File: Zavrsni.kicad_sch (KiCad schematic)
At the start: 37 parts, among them K1 JST-2pin-SMD, SW1 SW_Push, SW2 SW_Push

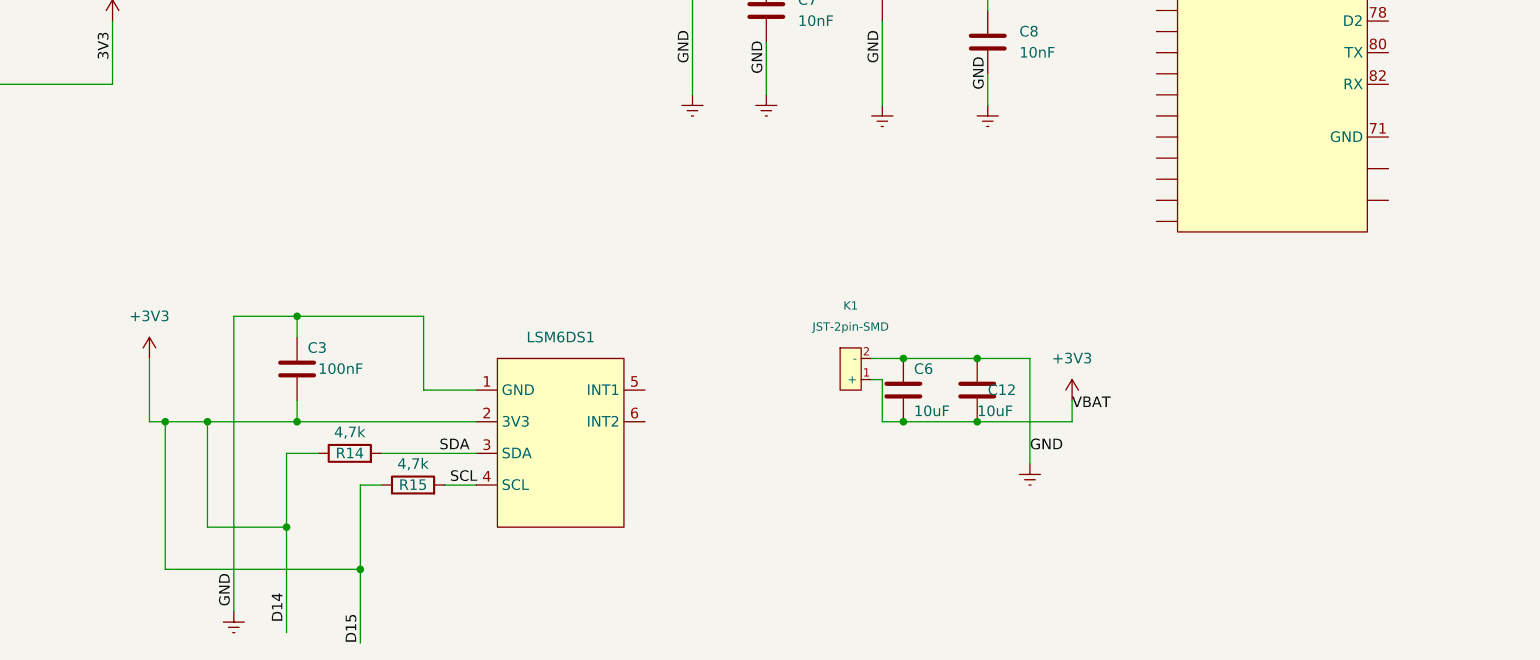
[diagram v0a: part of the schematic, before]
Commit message: All components on the PCB are connected
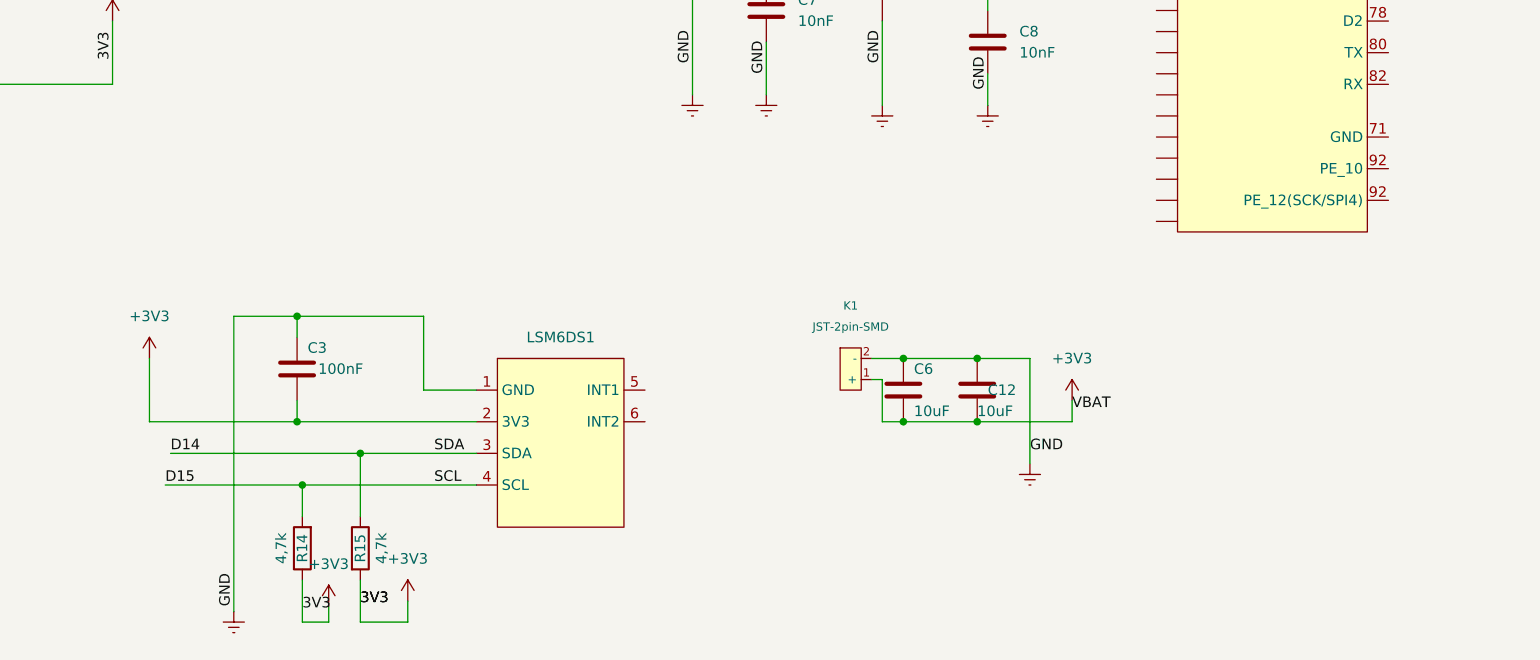
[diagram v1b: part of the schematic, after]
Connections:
- net +3.3V: now also R15.2; no longer NUCLEO_144_H743ZI2.48 (SCL), NUCLEO_144_H743ZI2.50 (SDA), R15.1
- net SCL renamed D15
- net D15: now also NUCLEO_144_H743ZI2.48 (SCL), R14.2; no longer R15.2
- net SDA renamed D14
- net D14: now also NUCLEO_144_H743ZI2.50 (SDA), R15.1; no longer R14.2
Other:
- moved on the sheet: R14, R15

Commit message: Add power switch, poligon for GND, and flip lsm on bottom
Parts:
- added C13, C14, C15: 10uF, Capacitor_SMD:C_1206_3216Metric, symbol Device:C
- added R7: 220K, Resistor_SMD:R_0603_1608Metric, symbol Device:R
- added SW3: Power_switch, Button_Switch_SMD:SW_DIP_SPSTx01_Slide_Omron_A6S-110x_W8.9mm_P2.54mm, symbol Switch:SW_Push
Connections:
- net +3.3V: now also C13.2, C14.1, C15.1, SW3.1
- net D: now also NMOS2.2 (D); no longer NMOS2.1 (D)
- net Earth: now also C13.1, C14.2, C15.2, R7.2
- net LED(PWM): now also NMOS2.1 (G); no longer NMOS2.2 (G)
- net INT1: now reaches LSM6DS1.5 (INT1)
- net INT1: now also NUCLEO_144_H743ZI2.2 (PC8)
- net INT2: now reaches LSM6DS1.6 (INT2)
- net INT2: now also NUCLEO_144_H743ZI2.4 (PC9)
- new net: R7.1, SW3.2
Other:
- moved on the sheet: C4

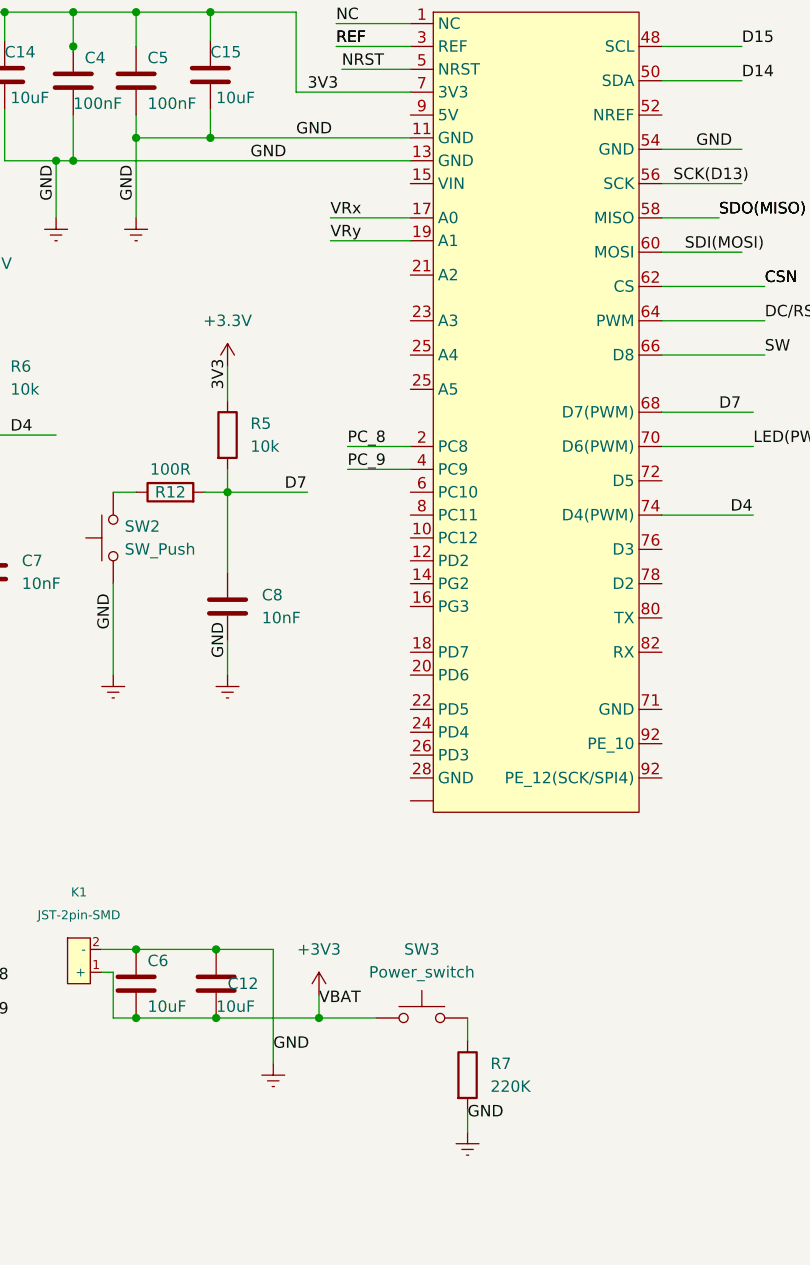
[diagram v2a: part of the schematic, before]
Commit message: switch error, the wrong switch was selected and connected incorrectly in the schematic
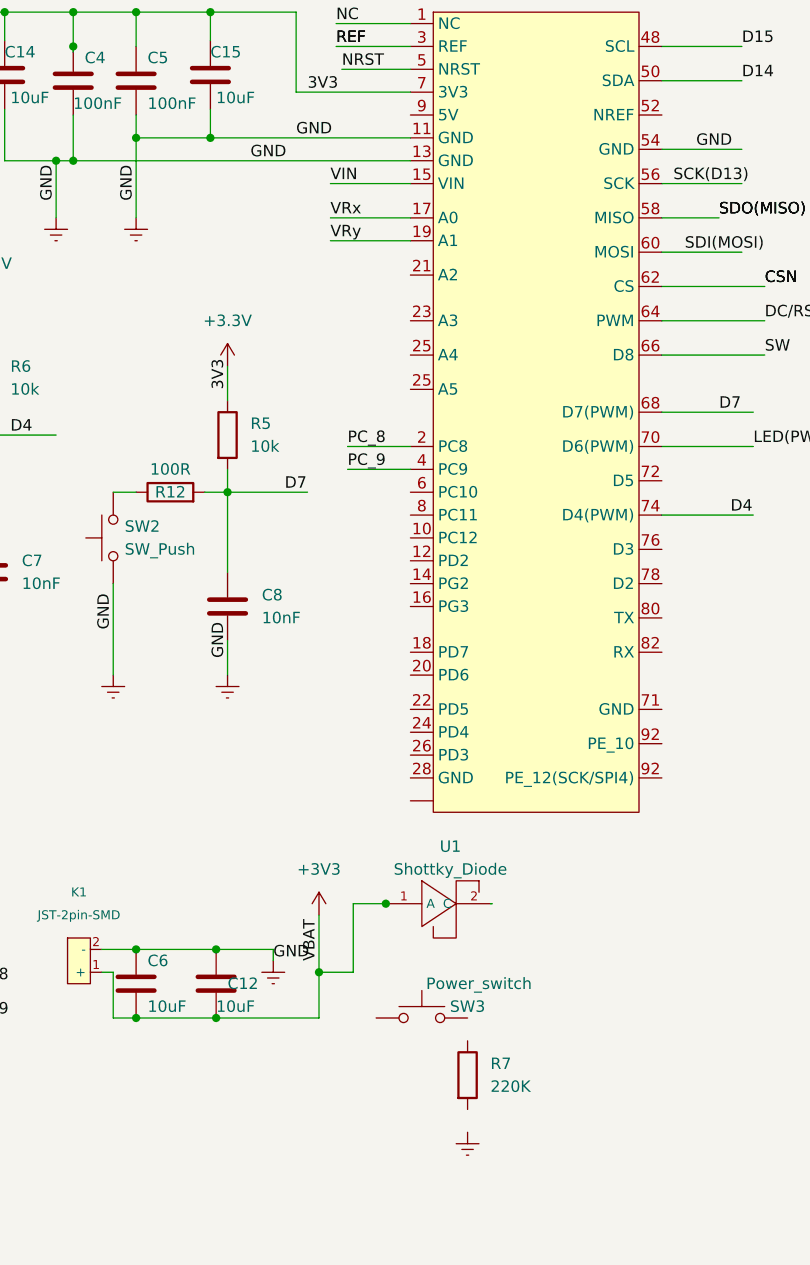
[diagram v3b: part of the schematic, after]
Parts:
- added U1: Shottky_Diode, Schottky_Diode:Sh_D bat20, symbol Shottky_diode:Shottky_Diode
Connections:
- net +3.3V: now also U1.1 (A); no longer SW3.1
- net Earth: no longer R7.2
- net at R7.1: no longer SW3.2
- net VIN: now reaches NUCLEO_144_H743ZI2.15 (VIN)
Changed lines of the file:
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@@
   (junction (at 214.63 88.9) (diameter 0) (color 0 0 0 0)
   )
-  (junction (at 224.79 147.32) (diameter 0) (color 0 0 0 0)
-  )
   (junction (at 204.47 147.32) (diameter 0) (color 0 0 0 0)
   )
@@
   (junction (at 153.67 39.37) (diameter 0) (color 0 0 0 0)
   )
+  (junction (at 232.22 134.62) (diameter 0) (color 0 0 0 0)
+  )
   (junction (at 62.23 45.72) (diameter 0) (color 0 0 0 0)
   )
+  (junction (at 224.79 142.24) (diameter 0) (color 0 0 0 0)
+  )
   (wire (pts (xy 213.36 147.32) (xy 224.79 147.32))
     (stroke (width 0) (type default))
@@
     (stroke (width 0) (type default))
   )
-  (wire (pts (xy 231.14 147.32) (xy 224.79 147.32))
-    (stroke (width 0) (type default))
-  )
   (wire (pts (xy 48.26 93.98) (xy 50.8 93.98))
     (stroke (width 0) (type default))
@@
     (stroke (width 0) (type default))
   )
-  (wire (pts (xy 241.3 147.32) (xy 241.3 149.86))
-    (stroke (width 0) (type default))
-  )
   (wire (pts (xy 226.06 58.42) (xy 234.95 58.42))
     (stroke (width 0) (type default))
@@
     (stroke (width 0) (type default))
   )
+  (wire (pts (xy 226.06 54.61) (xy 234.95 54.61))
+    (stroke (width 0) (type default))
+  )
   (wire (pts (xy 156.21 45.72) (xy 158.75 45.72))
     (stroke (width 0) (type default))
   )
-  (wire (pts (xy 224.79 144.78) (xy 224.79 147.32))
+  (wire (pts (xy 224.79 135.89) (xy 224.79 142.24))
     (stroke (width 0) (type default))
   )
@@
     (stroke (width 0) (type default))
   )
+  (wire (pts (xy 228.6 134.62) (xy 228.6 142.24))
+    (stroke (width 0) (type default))
+  )
   (wire (pts (xy 262.89 50.8) (xy 271.78 50.8))
     (stroke (width 0) (type default))
@@
     (stroke (width 0) (type default))
   )
+  (wire (pts (xy 228.6 142.24) (xy 224.79 142.24))
+    (stroke (width 0) (type default))
+  )
   (wire (pts (xy 158.75 45.72) (xy 163.83 45.72))
     (stroke (width 0) (type default))
@@
     (stroke (width 0) (type default))
   )
+  (wire (pts (xy 224.79 142.24) (xy 224.79 147.32))
+    (stroke (width 0) (type default))
+  )
   (wire (pts (xy 227.965 83.82) (xy 234.95 83.82))
     (stroke (width 0) (type default))
@@
     (stroke (width 0) (type default))
   )
+  (wire (pts (xy 228.6 134.62) (xy 232.22 134.62))
+    (stroke (width 0) (type default))
+  )
   (wire (pts (xy 212.725 35.56) (xy 212.725 38.735))
     (stroke (width 0) (type default))
@@
     (stroke (width 0) (type default))
   )
+  (wire (pts (xy 232.22 134.62) (xy 232.41 134.62))
+    (stroke (width 0) (type default))
+  )
   (wire (pts (xy 113.665 147.32) (xy 131.445 147.32))
     (stroke (width 0) (type default))
@@
     (stroke (width 0) (type default))
   )
+  (wire (pts (xy 243.84 134.62) (xy 244.03 134.62))
+    (stroke (width 0) (type default))
+  )
   (wire (pts (xy 226.06 60.96) (xy 234.95 60.96))
     (stroke (width 0) (type default))
@@
     (stroke (width 0) (type default))
   )
-  (wire (pts (xy 241.3 157.48) (xy 241.3 160.02))
-    (stroke (width 0) (type default))
-  )
   (wire (pts (xy 146.685 143.51) (xy 146.685 134.62))
     (stroke (width 0) (type default))
@@
     (stroke (width 0) (type default))
   )
-  (wire (pts (xy 219.71 139.7) (xy 219.71 152.4))
+  (wire (pts (xy 219.71 139.7) (xy 219.71 140.97))
     (stroke (width 0) (type default))
   )
@@
     (effects (font (size 1.27 1.27)) (justify left bottom))
   )
-  (label "GND" (at 219.71 151.13 0) (fields_autoplaced)
-    (effects (font (size 1.27 1.27)) (justify left bottom))
-  )
-  (label "GND" (at 241.3 158.75 0) (fields_autoplaced)
+  (label "GND" (at 219.71 140.97 0) (fields_autoplaced)
     (effects (font (size 1.27 1.27)) (justify left bottom))
   )
@@
   )
   (label "LED(PWM)" (at 273.05 83.82 0) (fields_autoplaced)
+    (effects (font (size 1.27 1.27)) (justify left bottom))
+  )
+  (label "VBAT" (at 224.79 140.97 90) (fields_autoplaced)
     (effects (font (size 1.27 1.27)) (justify left bottom))
   )
@@
     (effects (font (size 1.27 1.27)) (justify left bottom))
   )
-  (label "VBAT" (at 224.79 146.05 0) (fields_autoplaced)
+  (label "VIN" (at 226.06 54.61 0) (fields_autoplaced)
     (effects (font (size 1.27 1.27)) (justify left bottom))
   )
@@
         (path "/0b0be7ad-a3a6-4dc5-99d9-af21078bf390"
           (reference "R17") (unit 1)
+        )
+      )
+    )
+  )
+  (symbol (lib_id "Shottky_diode:Shottky_Diode") (at 238.76 134.62 0) (unit 1)
+    (in_bom yes) (on_board yes) (dnp no) (fields_autoplaced)
+    (property "Reference" "U1" (at 239.395 128.27 0)
+      (effects (font (size 1.27 1.27)))
+    )
+    (property "Value" "Shottky_Diode" (at 239.395 130.81 0)
+      (effects (font (size 1.27 1.27)))
+    )
+    (property "Footprint" "Schottky_Diode:Sh_D bat20" (at 238.76 134.62 0)
+      (effects (font (size 1.27 1.27)) hide)
+    )
+    (property "Datasheet" "" (at 238.76 134.62 0)
+      (effects (font (size 1.27 1.27)) hide)
+    )
+    (pin "1")
+    (pin "2")
+    (instances
+      (project "Zavrsni"
+        (path "/0b0be7ad-a3a6-4dc5-99d9-af21078bf390"
+          (reference "U1") (unit 1)
         )
       )
@@
   )
   (symbol (lib_id "Switch:SW_Push") (at 236.22 147.32 0) (unit 1)
-    (in_bom yes) (on_board yes) (dnp no) (fields_autoplaced)
-    (property "Reference" "SW3" (at 236.22 139.7 0)
-      (effects (font (size 1.27 1.27)))
-    )
-    (property "Value" "Power_switch" (at 236.22 142.24 0)
+    (in_bom yes) (on_board yes) (dnp no)
+    (property "Reference" "SW3" (at 241.3 146.05 0)
+      (effects (font (size 1.27 1.27)))
+    )
+    (property "Value" "Power_switch" (at 242.57 143.51 0)
       (effects (font (size 1.27 1.27)))
     )
@@
     )
   )
-  (symbol (lib_id "power:Earth") (at 219.71 152.4 0) (unit 1)
-    (in_bom yes) (on_board yes) (dnp no) (fields_autoplaced)
-    (property "Reference" "#PWR012" (at 219.71 158.75 0)
-      (effects (font (size 1.27 1.27)) hide)
-    )
-    (property "Value" "Earth" (at 219.71 156.21 0)
-      (effects (font (size 1.27 1.27)) hide)
-    )
-    (property "Footprint" "" (at 219.71 152.4 0)
-      (effects (font (size 1.27 1.27)) hide)
-    )
-    (property "Datasheet" "~" (at 219.71 152.4 0)
+  (symbol (lib_id "power:Earth") (at 219.71 140.97 0) (unit 1)
+    (in_bom yes) (on_board yes) (dnp no) (fields_autoplaced)
+    (property "Reference" "#PWR012" (at 219.71 147.32 0)
+      (effects (font (size 1.27 1.27)) hide)
+    )
+    (property "Value" "Earth" (at 219.71 144.78 0)
+      (effects (font (size 1.27 1.27)) hide)
+    )
+    (property "Footprint" "" (at 219.71 140.97 0)
+      (effects (font (size 1.27 1.27)) hide)
+    )
+    (property "Datasheet" "~" (at 219.71 140.97 0)
       (effects (font (size 1.27 1.27)) hide)
     )
@@
     )
   )
-  (symbol (lib_id "power:+3V3") (at 224.79 144.78 0) (unit 1)
-    (in_bom yes) (on_board yes) (dnp no) (fields_autoplaced)
-    (property "Reference" "#PWR09" (at 224.79 148.59 0)
-      (effects (font (size 1.27 1.27)) hide)
-    )
-    (property "Value" "+3V3" (at 224.79 139.7 0)
-      (effects (font (size 1.27 1.27)))
-    )
-    (property "Footprint" "" (at 224.79 144.78 0)
-      (effects (font (size 1.27 1.27)) hide)
-    )
-    (property "Datasheet" "" (at 224.79 144.78 0)
-      (effects (font (size 1.27 1.27)) hide)
-    )
+  (symbol (lib_id "power:+3V3") (at 224.79 135.89 0) (unit 1)
+    (in_bom yes) (on_board yes) (dnp no) (fields_autoplaced)
+    (property "Reference" "#PWR09" (at 224.79 139.7 0)
+      (effects (font (size 1.27 1.27)) hide)
+    )
+    (property "Value" "+3V3" (at 224.79 130.81 0)
+      (effects (font (size 1.27 1.27)))
+    )
+    (property "Footprint" "" (at 224.79 135.89 0)
+      (effects (font (size 1.27 1.27)) hide)
+    )
+    (property "Datasheet" "" (at 224.79 135.89 0)
+      (effects (font (size 1.27 1.27)) hide)
+    )

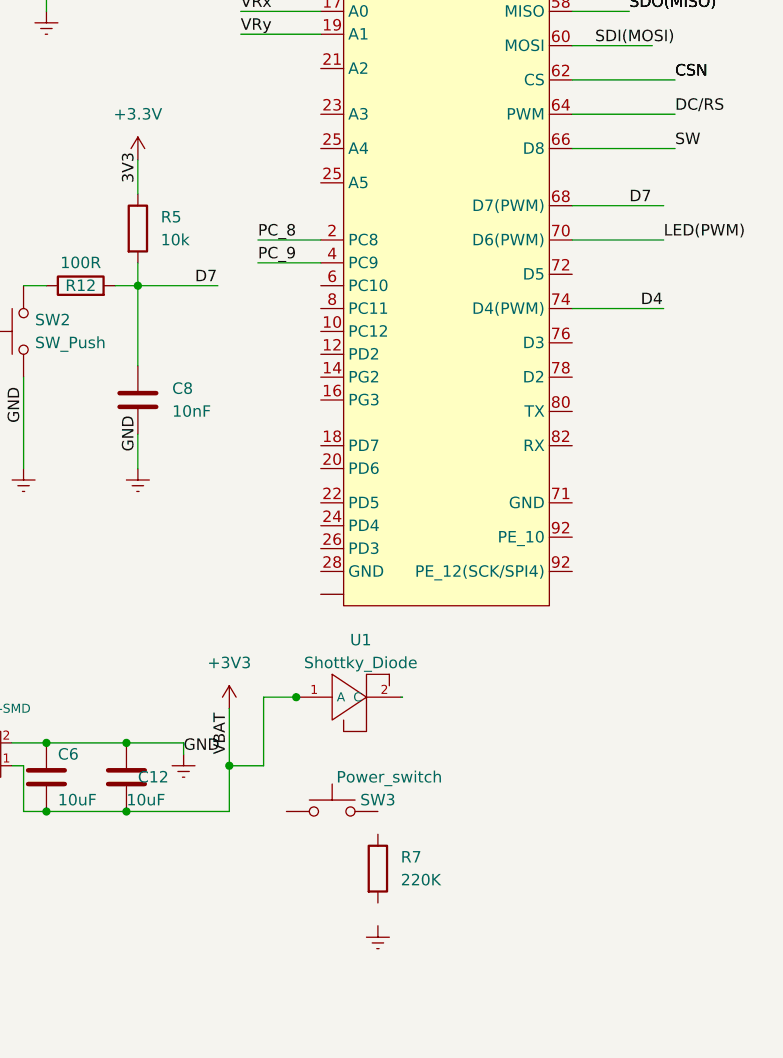
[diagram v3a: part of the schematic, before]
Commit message: Shifted pins on the nucleo board, up the y axis
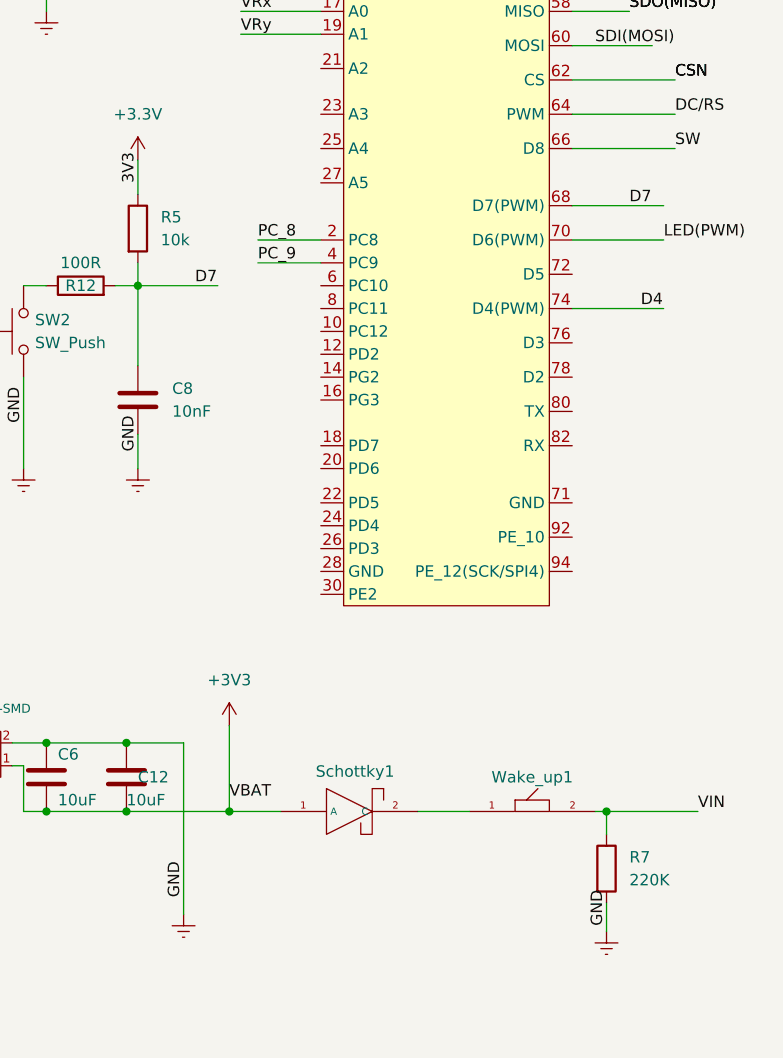
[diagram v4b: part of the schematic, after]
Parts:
- removed SW3: Power_switch, Button_Switch_SMD:SW_DIP_SPSTx01_Slide_Omron_A6S-110x_W8.9mm_P2.54mm, symbol Switch:SW_Push
- removed U1: Shottky_Diode, Schottky_Diode:Sh_D bat20, symbol Shottky_diode:Shottky_Diode
- added Schottky1: ~, Schottky_D:Schottky_D, symbol Schottky_Dsymbol:Schottky_D
- added Wake_up1: ~, Power_Switch:Power_Switch, symbol Power_Switch:P_SW
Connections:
- net +3.3V: now also Schottky1.1 (A)
- net Earth: now also R7.2
- net VIN: now also R7.1, Wake_up1.2
- new net: Schottky1.2 (C), Wake_up1.1
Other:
- moved on the sheet: R7
